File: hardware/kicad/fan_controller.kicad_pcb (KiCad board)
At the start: 2 copper layers, 100 x 80 mm, 0 parts

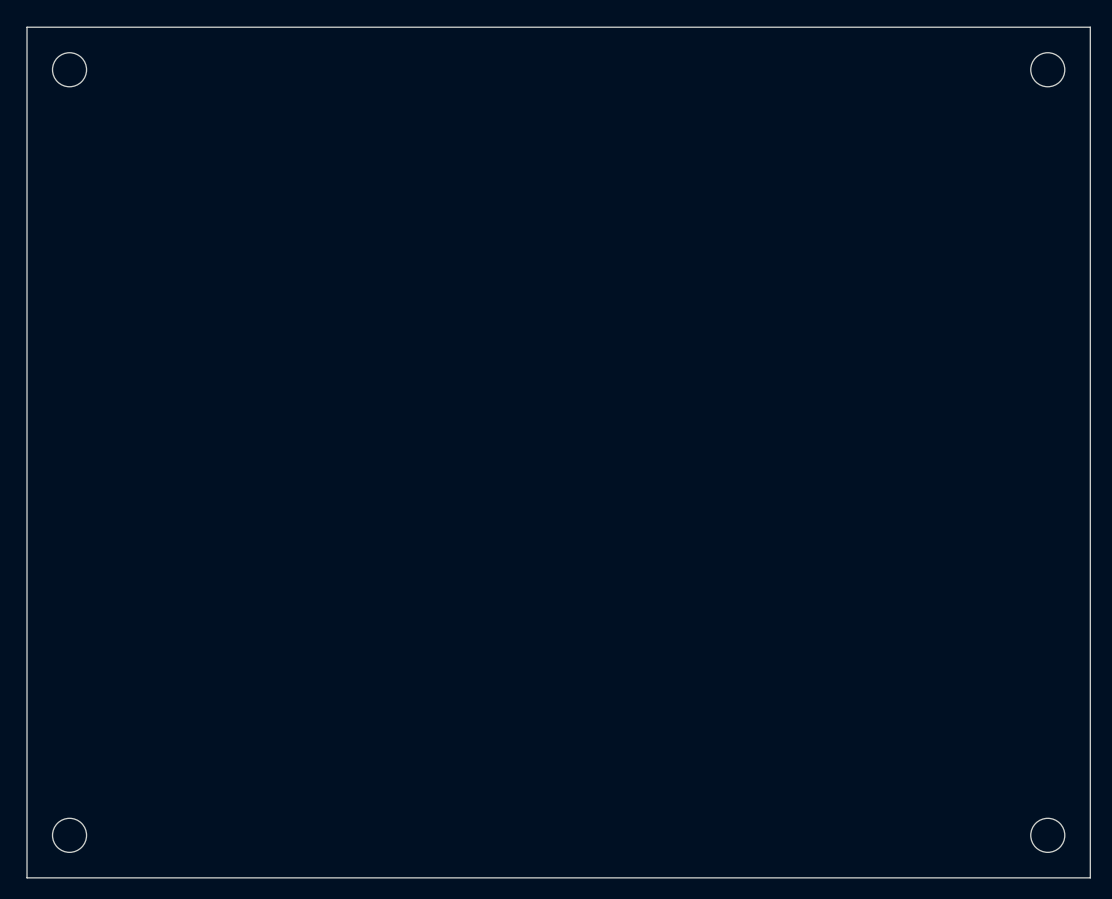
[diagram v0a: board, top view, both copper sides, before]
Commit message: hw: Blue Pill carrier, first placement and 3D model
The board is now a carrier for an STM32F103C8T6 Blue Pill module in two
1x20 sockets. The module brings the MCU, crystal, 3.3 V regulator, LED,
reset, BOOT jumpers, SWD and micro-B USB, so those parts are removed.
An AMS1117-5.0 feeds the module's 5V pin through an SS14, which stops
USB VBUS from back-feeding the regulator. R4 (DNP) corrects modules
whose D+ pull-up is 10k. Header pinout follows the DeepBlueMbedded
Blue Pill diagram.

place_pcb.py places every footprint by block (placed, not routed),
checks overlaps, board edges and mounting holes, and exports
fan_controller.step and .glb. The STEP models are committed under
hardware/kicad/3dmodels/ and referenced through ${KIPRJMOD}, so KiCad
uses them without the 3D library installed. pcb_top.png heads the
README.

Signed-off-by: Roman Skakun <rm.skakun@gmail.com>
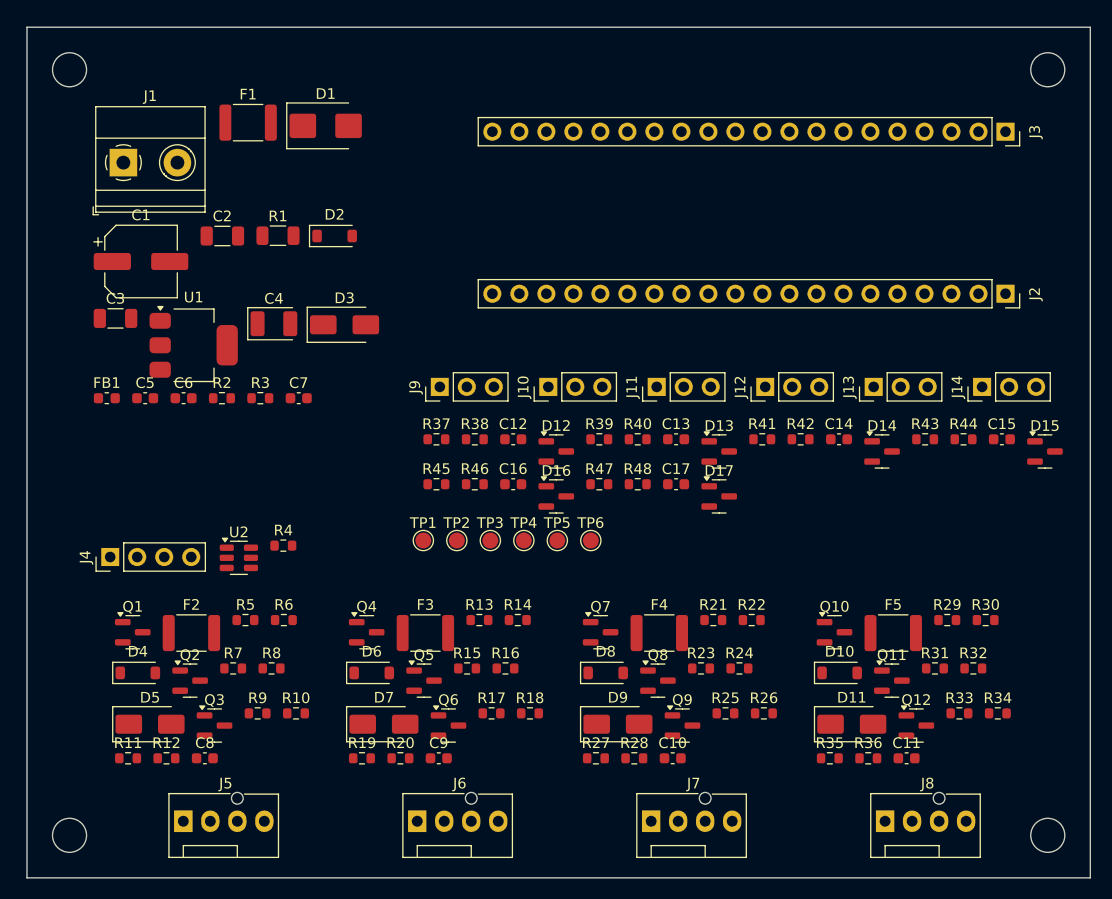
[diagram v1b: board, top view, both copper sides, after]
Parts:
- added C1: 100u 25V, Capacitor_SMD:CP_Elec_6.3x7.7, F.Cu at (10.7, 22.0)
- added C10: 1n, Capacitor_SMD:C_0603_1608Metric, F.Cu at (60.7, 68.8)
- added C11: 1n, Capacitor_SMD:C_0603_1608Metric, F.Cu at (82.7, 68.8)
- added C12: 100n, Capacitor_SMD:C_0603_1608Metric, F.Cu at (45.7, 38.8)
- added C13: 100n, Capacitor_SMD:C_0603_1608Metric, F.Cu at (61.0, 38.8)
- added C14: 100n, Capacitor_SMD:C_0603_1608Metric, F.Cu at (76.4, 38.8)
- added C15: 100n, Capacitor_SMD:C_0603_1608Metric, F.Cu at (91.7, 38.8)
- added C16: 100n, Capacitor_SMD:C_0603_1608Metric, F.Cu at (45.7, 43.0)
- added C17: 100n, Capacitor_SMD:C_0603_1608Metric, F.Cu at (61.0, 43.0)
- added C2: 10u 25V, Capacitor_SMD:C_1206_3216Metric, F.Cu at (18.4, 19.6)
- added C3: 10u 25V, Capacitor_SMD:C_1206_3216Metric, F.Cu at (8.32, 27.4)
- added C4: 22u 10V, Capacitor_Tantalum_SMD:CP_EIA-3528-21_Kemet-B, F.Cu at (23.2, 27.9)
- added C5: 1u, Capacitor_SMD:C_0603_1608Metric, F.Cu at (11.1, 34.9)
- added C6: 10n, Capacitor_SMD:C_0603_1608Metric, F.Cu at (14.7, 34.9)
- added C7: 100n, Capacitor_SMD:C_0603_1608Metric, F.Cu at (25.6, 34.9)
- added C8: 1n, Capacitor_SMD:C_0603_1608Metric, F.Cu at (16.7, 68.8)
- added C9: 1n, Capacitor_SMD:C_0603_1608Metric, F.Cu at (38.7, 68.8)
- added D1: SMBJ13A, Diode_SMD:D_SMB, F.Cu at (28.1, 9.28)
- added D10: BZT52C10, Diode_SMD:D_SOD-123, F.Cu at (76.4, 60.7)
- added D11: SS14, Diode_SMD:D_SMA, F.Cu at (77.6, 65.5)
- added D12: BAT54S, Package_TO_SOT_SMD:SOT-23, F.Cu at (49.8, 39.9)
- added D13: BAT54S, Package_TO_SOT_SMD:SOT-23, F.Cu at (65.1, 39.9)
- added D14: BAT54S, Package_TO_SOT_SMD:SOT-23, F.Cu at (80.4, 39.9)
- added D15: BAT54S, Package_TO_SOT_SMD:SOT-23, F.Cu at (95.7, 39.9)
- added D16: BAT54S, Package_TO_SOT_SMD:SOT-23, F.Cu at (49.8, 44.1)
- added D17: BAT54S, Package_TO_SOT_SMD:SOT-23, F.Cu at (65.1, 44.1)
- added D2: BZT52C13, Diode_SMD:D_SOD-123, F.Cu at (28.9, 19.6)
- added D3: SS14, Diode_SMD:D_SMA, F.Cu at (29.9, 28.0)
- added D4: BZT52C10, Diode_SMD:D_SOD-123, F.Cu at (10.4, 60.7)
- added D5: SS14, Diode_SMD:D_SMA, F.Cu at (11.6, 65.5)
- added D6: BZT52C10, Diode_SMD:D_SOD-123, F.Cu at (32.4, 60.7)
- added D7: SS14, Diode_SMD:D_SMA, F.Cu at (33.6, 65.5)
- added D8: BZT52C10, Diode_SMD:D_SOD-123, F.Cu at (54.4, 60.7)
- added D9: SS14, Diode_SMD:D_SMA, F.Cu at (55.6, 65.5)
- added F1: 2.5A, Fuse:Fuse_1812_4532Metric, F.Cu at (20.8, 8.97)
- added F2: 1.1A, Fuse:Fuse_1812_4532Metric, F.Cu at (15.5, 57.0)
- added F3: 1.1A, Fuse:Fuse_1812_4532Metric, F.Cu at (37.5, 57.0)
- added F4: 1.1A, Fuse:Fuse_1812_4532Metric, F.Cu at (59.5, 57.0)
- added F5: 1.1A, Fuse:Fuse_1812_4532Metric, F.Cu at (81.5, 57.0)
- added FB1: 600R@100MHz, Inductor_SMD:L_0603_1608Metric, F.Cu at (7.50, 34.9)
- added J1: 12V IN, TerminalBlock_Phoenix:TerminalBlock_Phoenix_MKDS-1,5-2-5.08_1x02_P5.08mm_Horizontal, F.Cu at (9.06, 12.7)
- added J10: AIN2, Connector_PinHeader_2.54mm:PinHeader_1x03_P2.54mm_Vertical, F.Cu at (49.0, 33.8)
- added J11: AIN3, Connector_PinHeader_2.54mm:PinHeader_1x03_P2.54mm_Vertical, F.Cu at (59.2, 33.8)
- added J12: AIN4, Connector_PinHeader_2.54mm:PinHeader_1x03_P2.54mm_Vertical, F.Cu at (69.4, 33.8)
- added J13: AIN5, Connector_PinHeader_2.54mm:PinHeader_1x03_P2.54mm_Vertical, F.Cu at (79.6, 33.8)
- added J14: AIN6, Connector_PinHeader_2.54mm:PinHeader_1x03_P2.54mm_Vertical, F.Cu at (89.8, 33.8)
- added J2: BluePill A, Connector_PinSocket_2.54mm:PinSocket_1x20_P2.54mm_Vertical, F.Cu at (92.0, 25.1)
- added J3: BluePill B, Connector_PinSocket_2.54mm:PinSocket_1x20_P2.54mm_Vertical, F.Cu at (92.0, 9.82)
- added J4: USB int, Connector_PinHeader_2.54mm:PinHeader_1x04_P2.54mm_Vertical, F.Cu at (7.83, 49.8)
- added J5: FAN1, Connector:FanPinHeader_1x04_P2.54mm_Vertical, F.Cu at (14.7, 74.7)
- added J6: FAN2, Connector:FanPinHeader_1x04_P2.54mm_Vertical, F.Cu at (36.7, 74.7)
- added J7: FAN3, Connector:FanPinHeader_1x04_P2.54mm_Vertical, F.Cu at (58.7, 74.7)
- added J8: FAN4, Connector:FanPinHeader_1x04_P2.54mm_Vertical, F.Cu at (80.7, 74.7)
- added J9: AIN1, Connector_PinHeader_2.54mm:PinHeader_1x03_P2.54mm_Vertical, F.Cu at (38.8, 33.8)
- added Q1: AO3401A, Package_TO_SOT_SMD:SOT-23, F.Cu at (9.95, 56.9)
- added Q10: AO3401A, Package_TO_SOT_SMD:SOT-23, F.Cu at (75.9, 56.9)
- added Q11: BSS138, Package_TO_SOT_SMD:SOT-23, F.Cu at (81.3, 61.5)
- added Q12: BSS138, Package_TO_SOT_SMD:SOT-23, F.Cu at (83.6, 65.7)
- added Q2: BSS138, Package_TO_SOT_SMD:SOT-23, F.Cu at (15.3, 61.5)
- added Q3: BSS138, Package_TO_SOT_SMD:SOT-23, F.Cu at (17.6, 65.7)
- added Q4: AO3401A, Package_TO_SOT_SMD:SOT-23, F.Cu at (31.9, 56.9)
- added Q5: BSS138, Package_TO_SOT_SMD:SOT-23, F.Cu at (37.3, 61.5)
- added Q6: BSS138, Package_TO_SOT_SMD:SOT-23, F.Cu at (39.6, 65.7)
- added Q7: AO3401A, Package_TO_SOT_SMD:SOT-23, F.Cu at (53.9, 56.9)
- added Q8: BSS138, Package_TO_SOT_SMD:SOT-23, F.Cu at (59.3, 61.5)
- added Q9: BSS138, Package_TO_SOT_SMD:SOT-23, F.Cu at (61.6, 65.7)
- added R1: 47, Resistor_SMD:R_1206_3216Metric, F.Cu at (23.6, 19.6)
- added R10: 100k, Resistor_SMD:R_0603_1608Metric, F.Cu at (25.3, 64.5)
- added R11: 10k, Resistor_SMD:R_0603_1608Metric, F.Cu at (9.50, 68.8)
- added R12: 1k, Resistor_SMD:R_0603_1608Metric, F.Cu at (13.1, 68.8)
- added R13: 4k7, Resistor_SMD:R_0603_1608Metric, F.Cu at (42.5, 55.8)
- added R14: 4k7, Resistor_SMD:R_0603_1608Metric, F.Cu at (46.2, 55.8)
- added R15: 100, Resistor_SMD:R_0603_1608Metric, F.Cu at (41.4, 60.3)
- added R16: 10k, Resistor_SMD:R_0603_1608Metric, F.Cu at (45.0, 60.3)
- added R17: 100, Resistor_SMD:R_0603_1608Metric, F.Cu at (43.7, 64.5)
- added R18: 100k, Resistor_SMD:R_0603_1608Metric, F.Cu at (47.3, 64.5)
- added R19: 10k, Resistor_SMD:R_0603_1608Metric, F.Cu at (31.5, 68.8)
- added R2: 47k, Resistor_SMD:R_0603_1608Metric, F.Cu at (18.3, 34.9)
- added R20: 1k, Resistor_SMD:R_0603_1608Metric, F.Cu at (35.1, 68.8)
- added R21: 4k7, Resistor_SMD:R_0603_1608Metric, F.Cu at (64.5, 55.8)
- added R22: 4k7, Resistor_SMD:R_0603_1608Metric, F.Cu at (68.2, 55.8)
- added R23: 100, Resistor_SMD:R_0603_1608Metric, F.Cu at (63.4, 60.3)
- added R24: 10k, Resistor_SMD:R_0603_1608Metric, F.Cu at (67.0, 60.3)
- added R25: 100, Resistor_SMD:R_0603_1608Metric, F.Cu at (65.7, 64.5)
- added R26: 100k, Resistor_SMD:R_0603_1608Metric, F.Cu at (69.3, 64.5)
- added R27: 10k, Resistor_SMD:R_0603_1608Metric, F.Cu at (53.5, 68.8)
- added R28: 1k, Resistor_SMD:R_0603_1608Metric, F.Cu at (57.1, 68.8)
- added R29: 4k7, Resistor_SMD:R_0603_1608Metric, F.Cu at (86.5, 55.8)
- added R3: 10k, Resistor_SMD:R_0603_1608Metric, F.Cu at (21.9, 34.9)
- added R30: 4k7, Resistor_SMD:R_0603_1608Metric, F.Cu at (90.2, 55.8)
- added R31: 100, Resistor_SMD:R_0603_1608Metric, F.Cu at (85.4, 60.3)
- added R32: 10k, Resistor_SMD:R_0603_1608Metric, F.Cu at (89.0, 60.3)
- added R33: 100, Resistor_SMD:R_0603_1608Metric, F.Cu at (87.7, 64.5)
- added R34: 100k, Resistor_SMD:R_0603_1608Metric, F.Cu at (91.3, 64.5)
- added R35: 10k, Resistor_SMD:R_0603_1608Metric, F.Cu at (75.5, 68.8)
- added R36: 1k, Resistor_SMD:R_0603_1608Metric, F.Cu at (79.1, 68.8)
- added R37: 10k, Resistor_SMD:R_0603_1608Metric, F.Cu at (38.5, 38.8)
- added R38: 1k, Resistor_SMD:R_0603_1608Metric, F.Cu at (42.1, 38.8)
- added R39: 10k, Resistor_SMD:R_0603_1608Metric, F.Cu at (53.8, 38.8)
- added R4: 1k8, Resistor_SMD:R_0603_1608Metric, F.Cu at (24.1, 48.8)
- added R40: 1k, Resistor_SMD:R_0603_1608Metric, F.Cu at (57.4, 38.8)
- added R41: 10k, Resistor_SMD:R_0603_1608Metric, F.Cu at (69.1, 38.8)
- added R42: 1k, Resistor_SMD:R_0603_1608Metric, F.Cu at (72.8, 38.8)
- added R43: 10k, Resistor_SMD:R_0603_1608Metric, F.Cu at (84.5, 38.8)
- added R44: 1k, Resistor_SMD:R_0603_1608Metric, F.Cu at (88.1, 38.8)
- added R45: 10k, Resistor_SMD:R_0603_1608Metric, F.Cu at (38.5, 43.0)
- added R46: 1k, Resistor_SMD:R_0603_1608Metric, F.Cu at (42.1, 43.0)
- added R47: 10k, Resistor_SMD:R_0603_1608Metric, F.Cu at (53.8, 43.0)
- added R48: 1k, Resistor_SMD:R_0603_1608Metric, F.Cu at (57.4, 43.0)
- added R5: 4k7, Resistor_SMD:R_0603_1608Metric, F.Cu at (20.5, 55.8)
- added R6: 4k7, Resistor_SMD:R_0603_1608Metric, F.Cu at (24.2, 55.8)
- added R7: 100, Resistor_SMD:R_0603_1608Metric, F.Cu at (19.4, 60.3)
- added R8: 10k, Resistor_SMD:R_0603_1608Metric, F.Cu at (23.0, 60.3)
- added R9: 100, Resistor_SMD:R_0603_1608Metric, F.Cu at (21.7, 64.5)
- added TP1: +12V, TestPoint:TestPoint_Pad_D1.5mm, F.Cu at (37.3, 48.3)
- added TP2: +3V3, TestPoint:TestPoint_Pad_D1.5mm, F.Cu at (40.4, 48.3)
- added TP3: GND, TestPoint:TestPoint_Pad_D1.5mm, F.Cu at (43.6, 48.3)
- added TP4: NRST, TestPoint:TestPoint_Pad_D1.5mm, F.Cu at (46.7, 48.3)
- added TP5: FAN1_PWM, TestPoint:TestPoint_Pad_D1.5mm, F.Cu at (49.9, 48.3)
- added TP6: FAN1_TACH, TestPoint:TestPoint_Pad_D1.5mm, F.Cu at (53.0, 48.3)
- added U1: AMS1117-5.0, Package_TO_SOT_SMD:SOT-223-3_TabPin2, F.Cu at (15.7, 29.9)
- added U2: USBLC6-2SC6, Package_TO_SOT_SMD:SOT-23-6, F.Cu at (19.9, 49.9)

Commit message: hw: power Blue Pill from USB, feed fans straight from 12 V
The Blue Pill now runs from USB only, so the AMS1117-5.0 and its
protection (47 R, 13 V zener, tantalum, SS14 OR diode) are removed.

Fan pin 2 connects to +12 V through its 1.1 A PTC. The high-side
P-FET, its gate network, level shifter and freewheel diode are gone
from every channel. Fans now run at 100 % whenever the module is
unpowered, held in reset or missing, because the PWM buffer releases
the line. Before, unplugging USB would have switched every fan off.
3-pin fans and the hard stop at 0 % are no longer supported.

Firmware 2.0 drops TIM2 and the mode command; get no longer prints
mode=. fanctl.py drops its mode subcommand.

The board shrinks from 100 x 80 mm to 75 x 60 mm and from 122 to 84
parts. Board size now lives in gen_kicad.py and is shared with
place_pcb.py. Placement, STEP, GLB and renders are regenerated, and
unused 3D models are removed. README replaces the safety prose with
a failure-case table.

Signed-off-by: Roman Skakun <rm.skakun@gmail.com>
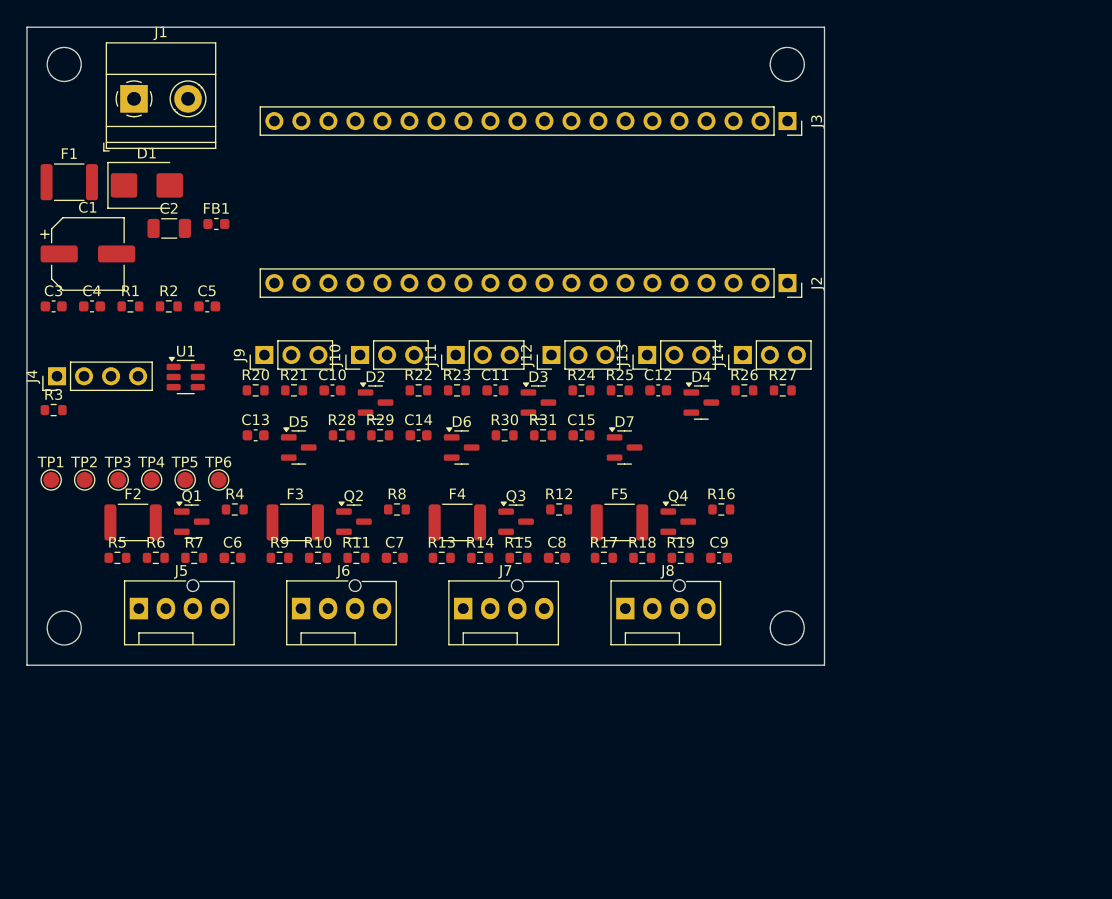
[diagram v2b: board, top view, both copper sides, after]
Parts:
- removed C16, C17: 100n, Capacitor_SMD:C_0603_1608Metric
- removed D10, D8: BZT52C10, Diode_SMD:D_SOD-123
- removed D11, D9: SS14, Diode_SMD:D_SMA
- removed D12, D13, D14, D15, D16, D17: BAT54S, Package_TO_SOT_SMD:SOT-23
- removed Q10, Q7: AO3401A, Package_TO_SOT_SMD:SOT-23
- removed Q11, Q12, Q5, Q6, Q8, Q9: BSS138, Package_TO_SOT_SMD:SOT-23
- removed R32, R35, R37, R39, R41, R43, R45, R47: 10k, Resistor_SMD:R_0603_1608Metric
- removed R33: 100, Resistor_SMD:R_0603_1608Metric
- removed R34: 100k, Resistor_SMD:R_0603_1608Metric
- removed R36, R38, R40, R42, R44, R46, R48: 1k, Resistor_SMD:R_0603_1608Metric
- removed U2: USBLC6-2SC6, Package_TO_SOT_SMD:SOT-23-6
- C10, C11: value 1n -> 100n
- C3: value 10u 25V -> 1u; footprint Capacitor_SMD:C_1206_3216Metric -> Capacitor_SMD:C_0603_1608Metric
- C4: value 22u 10V -> 10n; footprint Capacitor_Tantalum_SMD:CP_EIA-3528-21_Kemet-B -> Capacitor_SMD:C_0603_1608Metric
- C5: value 1u -> 100n
- C6: value 10n -> 1n
- C7: value 100n -> 1n
- D2: value BZT52C13 -> BAT54S; footprint Diode_SMD:D_SOD-123 -> Package_TO_SOT_SMD:SOT-23
- D3, D5, D7: value SS14 -> BAT54S; footprint Diode_SMD:D_SMA -> Package_TO_SOT_SMD:SOT-23
- D4, D6: value BZT52C10 -> BAT54S; footprint Diode_SMD:D_SOD-123 -> Package_TO_SOT_SMD:SOT-23
- Q1, Q4: value AO3401A -> BSS138
- R1: value 47 -> 47k; footprint Resistor_SMD:R_1206_3216Metric -> Resistor_SMD:R_0603_1608Metric
- R10, R18, R26: value 100k -> 10k
- R11, R19, R27: value 10k -> 1k
- R12: value 1k -> 100
- R13, R5: value 4k7 -> 100k
- R14, R22, R30, R6: value 4k7 -> 10k
- R15, R23, R25, R31, R7: value 100 -> 1k
- R16, R8: value 10k -> 100
- R17, R9: value 100 -> 100k
- R2: value 47k -> 10k
- R20, R28: value 1k -> 10k
- R21, R29: value 4k7 -> 1k
- R3: value 10k -> 1k8
- R4: value 1k8 -> 100
- U1: value AMS1117-5.0 -> USBLC6-2SC6; footprint Package_TO_SOT_SMD:SOT-223-3_TabPin2 -> Package_TO_SOT_SMD:SOT-23-6
- moved D4 58.8 mm to (63.4, 35.3)
- moved R29 56.1 mm to (33.2, 38.4)
- moved C11 51.9 mm to (44.0, 34.2)
- moved R30 48.5 mm to (44.9, 38.4)
- moved C10 47.1 mm to (28.7, 34.2)
- moved R21 45.0 mm to (25.1, 34.2)
- moved R12 43.7 mm to (50.0, 45.4)
- moved R31 42.9 mm to (48.5, 38.4)
- moved R28 41.0 mm to (29.6, 38.4)
- moved C13 39.5 mm to (21.5, 38.4)
- moved C14 39.5 mm to (36.8, 38.4)
- moved C15 39.5 mm to (52.1, 38.4)
- moved R27 38.8 mm to (71.1, 34.2)
- moved C8 38.1 mm to (49.8, 49.9)
- moved R22 38.1 mm to (36.8, 34.2)
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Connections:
- C10 pad 1: FAN3_TACH -> AIN1
- C11 pad 1: FAN4_TACH -> AIN2
- C12 pad 1: AIN1 -> AIN3
- C13 pad 1: AIN2 -> AIN4
- C14 pad 1: AIN3 -> AIN5
- C15 pad 1: AIN4 -> AIN6
- C3 pad 1: VREG_IN -> +3V3A
- C4 pad 1: +5V_REG -> +3V3A
- C5 pad 1: +3V3A -> V12_SENSE
- C6 pad 1: +3V3A -> FAN1_TACH
- C7 pad 1: V12_SENSE -> FAN2_TACH
- C8 pad 1: FAN1_TACH -> FAN3_TACH
- C9 pad 1: FAN2_TACH -> FAN4_TACH
- D2 pad 1: VREG_IN -> GND
- D2 pad 2: GND -> +3V3A
- D3 pad 1: +5V -> GND
- D3 pad 2: +5V_REG -> +3V3A
- D4 pad 1: +12V -> GND
- D4 pad 2: FAN1_GATE -> +3V3A
- D5 pad 1: FAN1_12V -> GND
- D5 pad 2: GND -> +3V3A
- D6 pad 1: +12V -> GND
- D6 pad 2: FAN2_GATE -> +3V3A
- D7 pad 1: FAN2_12V -> GND
- D7 pad 2: GND -> +3V3A
- F2 pad 1: FAN1_SW_12V -> +12V
- F3 pad 1: FAN2_SW_12V -> +12V
- F4 pad 1: FAN3_SW_12V -> +12V
- F5 pad 1: FAN4_SW_12V -> +12V
- J2 pad 5: FAN4_PWR -> (no net)
- J2 pad 6: FAN3_PWR -> (no net)
- J3 pad 10: FAN1_PWR -> (no net)
- J3 pad 11: FAN2_PWR -> (no net)
- Q1 pad 1: FAN1_GATE -> FAN1_PWM_G
- Q1 pad 2: +12V -> GND
- Q1 pad 3: FAN1_SW_12V -> FAN1_PWM_OUT
- Q2 pad 1: FAN1_PWR_G -> FAN2_PWM_G
- Q2 pad 3: FAN1_DRV -> FAN2_PWM_OUT
- Q3 pad 1: FAN1_PWM_G -> FAN3_PWM_G
- Q3 pad 3: FAN1_PWM_OUT -> FAN3_PWM_OUT
- Q4 pad 1: FAN2_GATE -> FAN4_PWM_G
- Q4 pad 2: +12V -> GND
- Q4 pad 3: FAN2_SW_12V -> FAN4_PWM_OUT
- R1 pad 2: VREG_IN -> V12_SENSE
- R10 pad 1: FAN1_PWM_G -> FAN2_TACH_IN
- R10 pad 2: GND -> +3V3
- R11 pad 1: FAN1_TACH_IN -> FAN2_TACH_IN
- R11 pad 2: +3V3 -> FAN2_TACH
- R12 pad 1: FAN1_TACH_IN -> FAN3_PWM
- R12 pad 2: FAN1_TACH -> FAN3_PWM_G
- R13 pad 1: +12V -> FAN3_PWM_G
- R13 pad 2: FAN2_GATE -> GND
- R14 pad 1: FAN2_GATE -> FAN3_TACH_IN
- R14 pad 2: FAN2_DRV -> +3V3
- R15 pad 1: FAN2_PWR -> FAN3_TACH_IN
- R15 pad 2: FAN2_PWR_G -> FAN3_TACH
- R16 pad 1: FAN2_PWR_G -> FAN4_PWM
- R16 pad 2: +3V3 -> FAN4_PWM_G
- R17 pad 1: FAN2_PWM -> FAN4_PWM_G
- R17 pad 2: FAN2_PWM_G -> GND
- R18 pad 1: FAN2_PWM_G -> FAN4_TACH_IN
- R18 pad 2: GND -> +3V3
- R19 pad 1: FAN2_TACH_IN -> FAN4_TACH_IN
- R19 pad 2: +3V3 -> FAN4_TACH
- R2 pad 1: +12V -> V12_SENSE
- R2 pad 2: V12_SENSE -> GND
- R20 pad 1: FAN2_TACH_IN -> AIN1_IN
- R20 pad 2: FAN2_TACH -> +3V3A
- R21 pad 1: +12V -> AIN1_IN
- R21 pad 2: FAN3_GATE -> AIN1
- R22 pad 1: FAN3_GATE -> AIN2_IN
- R22 pad 2: FAN3_DRV -> +3V3A
- R23 pad 1: FAN3_PWR -> AIN2_IN
- R23 pad 2: FAN3_PWR_G -> AIN2
- R24 pad 1: FAN3_PWR_G -> AIN3_IN
- R24 pad 2: +3V3 -> +3V3A
- R25 pad 1: FAN3_PWM -> AIN3_IN
- R25 pad 2: FAN3_PWM_G -> AIN3
- R26 pad 1: FAN3_PWM_G -> AIN4_IN
- R26 pad 2: GND -> +3V3A
- R27 pad 1: FAN3_TACH_IN -> AIN4_IN
- R27 pad 2: +3V3 -> AIN4
- R28 pad 1: FAN3_TACH_IN -> AIN5_IN
- R28 pad 2: FAN3_TACH -> +3V3A
- R29 pad 1: +12V -> AIN5_IN
- R29 pad 2: FAN4_GATE -> AIN5
- R3 pad 1: V12_SENSE -> USB_DP
- R3 pad 2: GND -> +3V3
- R30 pad 1: FAN4_GATE -> AIN6_IN
- R30 pad 2: FAN4_DRV -> +3V3A
- R31 pad 1: FAN4_PWR -> AIN6_IN
- R31 pad 2: FAN4_PWR_G -> AIN6
- R4 pad 1: USB_DP -> FAN1_PWM
- R4 pad 2: +3V3 -> FAN1_PWM_G
- R5 pad 1: +12V -> FAN1_PWM_G
- R5 pad 2: FAN1_GATE -> GND
- R6 pad 1: FAN1_GATE -> FAN1_TACH_IN
- R6 pad 2: FAN1_DRV -> +3V3
- R7 pad 1: FAN1_PWR -> FAN1_TACH_IN
- R7 pad 2: FAN1_PWR_G -> FAN1_TACH
- R8 pad 1: FAN1_PWR_G -> FAN2_PWM
- R8 pad 2: +3V3 -> FAN2_PWM_G
- R9 pad 1: FAN1_PWM -> FAN2_PWM_G
- R9 pad 2: FAN1_PWM_G -> GND
- U1 pad 1: GND -> USB_DP
- U1 pad 2: +5V_REG -> GND
- U1 pad 3: VREG_IN -> USB_DM
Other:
- board size 100 x 80 mm -> 75 x 60 mm
